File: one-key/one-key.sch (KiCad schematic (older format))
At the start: 8 parts, among them J2 Conn_01x04, SW1 SW_Push, U1 C8051F38x_32

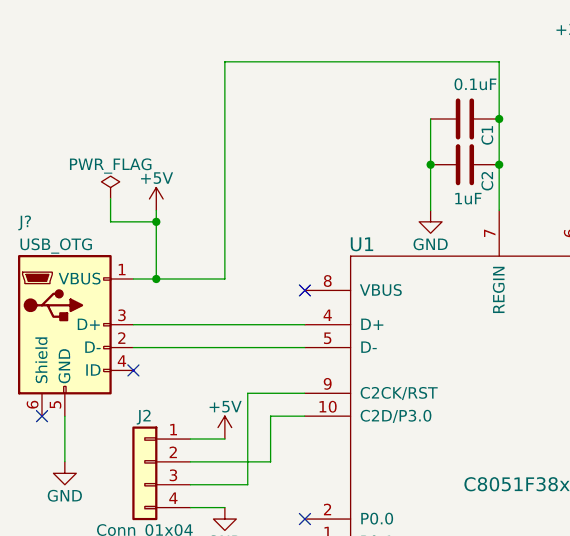
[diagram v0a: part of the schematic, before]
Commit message: vbus sense pin needs to be connected
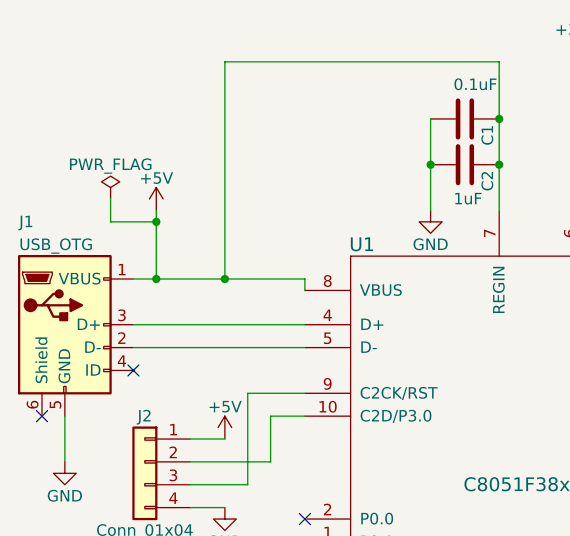
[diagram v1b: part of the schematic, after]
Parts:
- gave numbers to parts that had none: 1
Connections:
- net +5V: now also U1.8 (VBUS)
- no-connect marks 26 -> 25
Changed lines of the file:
@@
 $EndComp
 $Comp
-L GND #PWR01
+L GND #PWR9
 U 1 1 59BC69D8
 P 5000 1750
-F 0 "#PWR01" H 5000 1500 50  0001 C CNN
+F 0 "#PWR9" H 5000 1500 50  0001 C CNN
 F 1 "GND" H 5000 1600 50  0000 C CNN
 F 2 "" H 5000 1750 50  0001 C CNN
@@
 $EndComp
 $Comp
-L GND #PWR02
+L GND #PWR6
 U 1 1 59BC6AED
 P 4050 1750
-F 0 "#PWR02" H 4050 1500 50  0001 C CNN
+F 0 "#PWR6" H 4050 1500 50  0001 C CNN
 F 1 "GND" H 4050 1600 50  0000 C CNN
 F 2 "" H 4050 1750 50  0001 C CNN
@@
 $EndComp
 $Comp
-L +3.3V #PWR03
+L +3.3V #PWR8
 U 1 1 59BC6B24
 P 4700 1100
-F 0 "#PWR03" H 4700 950 50  0001 C CNN
+F 0 "#PWR8" H 4700 950 50  0001 C CNN
 F 1 "+3.3V" H 4700 1240 50  0000 C CNN
 F 2 "" H 4700 1100 50  0001 C CNN
@@
 NoConn ~ 2350 2650
 $Comp
-L GND #PWR04
+L GND #PWR1
 U 1 1 59BC6CDD
 P 2450 2850
-F 0 "#PWR04" H 2450 2600 50  0001 C CNN
+F 0 "#PWR1" H 2450 2600 50  0001 C CNN
 F 1 "GND" H 2450 2700 50  0000 C CNN
 F 2 "" H 2450 2850 50  0001 C CNN
@@
 	1    0    0    -1
 $EndComp
-NoConn ~ 3500 2100
-$Comp
-L GND #PWR05
+$Comp
+L GND #PWR7
 U 1 1 59BC6D91
 P 4500 4350
-F 0 "#PWR05" H 4500 4100 50  0001 C CNN
+F 0 "#PWR7" H 4500 4100 50  0001 C CNN
 F 1 "GND" H 4500 4200 50  0000 C CNN
 F 2 "" H 4500 4350 50  0001 C CNN
@@
 $EndComp
 $Comp
-L GND #PWR06
+L GND #PWR5
 U 1 1 59BC8562
 P 3150 3050
-F 0 "#PWR06" H 3150 2800 50  0001 C CNN
+F 0 "#PWR5" H 3150 2800 50  0001 C CNN
 F 1 "GND" H 3150 2900 50  0000 C CNN
 F 2 "" H 3150 3050 50  0001 C CNN
@@
 $EndComp
 $Comp
-L GND #PWR07
+L GND #PWR2
 U 1 1 59BC8C94
 P 2500 3800
-F 0 "#PWR07" H 2500 3550 50  0001 C CNN
+F 0 "#PWR2" H 2500 3550 50  0001 C CNN
 F 1 "GND" H 2500 3650 50  0000 C CNN
 F 2 "" H 2500 3800 50  0001 C CNN
@@
 	2500 3650 2500 3800
 $Comp
-L +5V #PWR08
+L +5V #PWR3
 U 1 1 59BC8F84
 P 2850 1750
-F 0 "#PWR08" H 2850 1600 50  0001 C CNN
+F 0 "#PWR3" H 2850 1600 50  0001 C CNN
 F 1 "+5V" H 2850 1890 50  0000 C CNN
 F 2 "" H 2850 1750 50  0001 C CNN
@@
 	3150 1100 3150 2050
 Wire Wire Line
-	3150 2050 2750 2050
+	2750 2050 3500 2050
 Wire Wire Line
 	2850 1750 2850 2050
 Connection ~ 2850 2050
 $Comp
-L PWR_FLAG #FLG09
+L PWR_FLAG #FLG1
 U 1 1 59BC904D
 P 2650 1700
-F 0 "#FLG09" H 2650 1775 50  0001 C CNN
+F 0 "#FLG1" H 2650 1775 50  0001 C CNN
 F 1 "PWR_FLAG" H 2650 1850 50  0000 C CNN
 F 2 "" H 2650 1700 50  0001 C CNN
@@
 Connection ~ 2850 1800
 $Comp
-L +5V #PWR010
+L +5V #PWR4
 U 1 1 59BC90F8
 P 3150 2750
-F 0 "#PWR010" H 3150 2600 50  0001 C CNN
+F 0 "#PWR4" H 3150 2600 50  0001 C CNN
 F 1 "+5V" H 3150 2890 50  0000 C CNN
 F 2 "" H 3150 2750 50  0001 C CNN
@@
 	3300 3200 3500 3200
 $Comp
-L USB_OTG J?
+L USB_OTG J1
 U 1 1 59BC971A
 P 2450 2250
-F 0 "J?" H 2250 2700 50  0000 L CNN
+F 0 "J1" H 2250 2700 50  0000 L CNN
 F 1 "USB_OTG" H 2250 2600 50  0000 L CNN
 F 2 "" H 2600 2200 50  0001 C CNN
@@
 	1    0    0    -1
 $EndComp
+Wire Wire Line
+	3500 2050 3500 2100
+Connection ~ 3150 2050
 $EndSCHEMATC

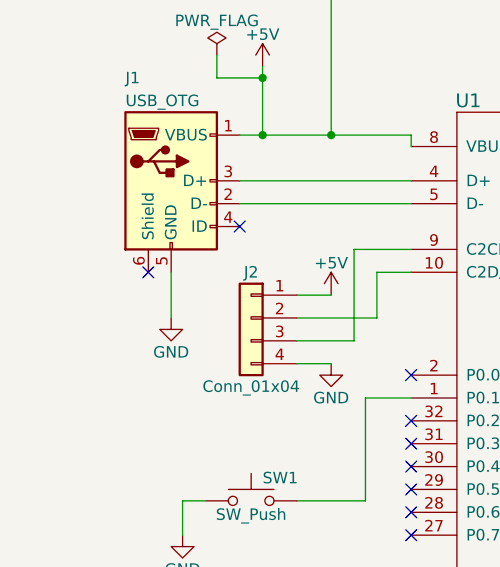
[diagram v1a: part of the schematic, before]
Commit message: add images and license text
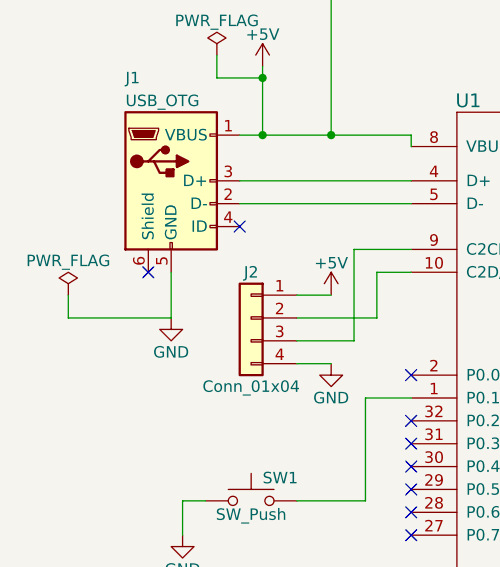
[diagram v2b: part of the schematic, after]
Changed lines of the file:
@@
 $EndComp
 $Comp
-L GND #PWR9
+L GND #PWR01
 U 1 1 59BC69D8
 P 5000 1750
-F 0 "#PWR9" H 5000 1500 50  0001 C CNN
+F 0 "#PWR01" H 5000 1500 50  0001 C CNN
 F 1 "GND" H 5000 1600 50  0000 C CNN
 F 2 "" H 5000 1750 50  0001 C CNN
@@
 $EndComp
 $Comp
-L GND #PWR6
+L GND #PWR02
 U 1 1 59BC6AED
 P 4050 1750
-F 0 "#PWR6" H 4050 1500 50  0001 C CNN
+F 0 "#PWR02" H 4050 1500 50  0001 C CNN
 F 1 "GND" H 4050 1600 50  0000 C CNN
 F 2 "" H 4050 1750 50  0001 C CNN
@@
 $EndComp
 $Comp
-L +3.3V #PWR8
+L +3.3V #PWR03
 U 1 1 59BC6B24
 P 4700 1100
-F 0 "#PWR8" H 4700 950 50  0001 C CNN
+F 0 "#PWR03" H 4700 950 50  0001 C CNN
 F 1 "+3.3V" H 4700 1240 50  0000 C CNN
 F 2 "" H 4700 1100 50  0001 C CNN
@@
 NoConn ~ 2350 2650
 $Comp
-L GND #PWR1
+L GND #PWR04
 U 1 1 59BC6CDD
 P 2450 2850
-F 0 "#PWR1" H 2450 2600 50  0001 C CNN
+F 0 "#PWR04" H 2450 2600 50  0001 C CNN
 F 1 "GND" H 2450 2700 50  0000 C CNN
 F 2 "" H 2450 2850 50  0001 C CNN
@@
 $EndComp
 $Comp
-L GND #PWR7
+L GND #PWR05
 U 1 1 59BC6D91
 P 4500 4350
-F 0 "#PWR7" H 4500 4100 50  0001 C CNN
+F 0 "#PWR05" H 4500 4100 50  0001 C CNN
 F 1 "GND" H 4500 4200 50  0000 C CNN
 F 2 "" H 4500 4350 50  0001 C CNN
@@
 $EndComp
 $Comp
-L GND #PWR5
+L GND #PWR06
 U 1 1 59BC8562
 P 3150 3050
-F 0 "#PWR5" H 3150 2800 50  0001 C CNN
+F 0 "#PWR06" H 3150 2800 50  0001 C CNN
 F 1 "GND" H 3150 2900 50  0000 C CNN
 F 2 "" H 3150 3050 50  0001 C CNN
@@
 $EndComp
 $Comp
-L GND #PWR2
+L GND #PWR07
 U 1 1 59BC8C94
 P 2500 3800
-F 0 "#PWR2" H 2500 3550 50  0001 C CNN
+F 0 "#PWR07" H 2500 3550 50  0001 C CNN
 F 1 "GND" H 2500 3650 50  0000 C CNN
 F 2 "" H 2500 3800 50  0001 C CNN
@@
 	2500 3650 2500 3800
 $Comp
-L +5V #PWR3
+L +5V #PWR08
 U 1 1 59BC8F84
 P 2850 1750
-F 0 "#PWR3" H 2850 1600 50  0001 C CNN
+F 0 "#PWR08" H 2850 1600 50  0001 C CNN
 F 1 "+5V" H 2850 1890 50  0000 C CNN
 F 2 "" H 2850 1750 50  0001 C CNN
@@
 Connection ~ 2850 2050
 $Comp
-L PWR_FLAG #FLG1
+L PWR_FLAG #FLG09
 U 1 1 59BC904D
 P 2650 1700
-F 0 "#FLG1" H 2650 1775 50  0001 C CNN
+F 0 "#FLG09" H 2650 1775 50  0001 C CNN
 F 1 "PWR_FLAG" H 2650 1850 50  0000 C CNN
 F 2 "" H 2650 1700 50  0001 C CNN
@@
 Connection ~ 2850 1800
 $Comp
-L +5V #PWR4
+L +5V #PWR010
 U 1 1 59BC90F8
 P 3150 2750
-F 0 "#PWR4" H 3150 2600 50  0001 C CNN
+F 0 "#PWR010" H 3150 2600 50  0001 C CNN
 F 1 "+5V" H 3150 2890 50  0000 C CNN
 F 2 "" H 3150 2750 50  0001 C CNN
@@
 	3500 2050 3500 2100
 Connection ~ 3150 2050
+$Comp
+L PWR_FLAG #FLG011
+U 1 1 59BDFC11
+P 2000 2750
+F 0 "#FLG011" H 2000 2825 50  0001 C CNN
+F 1 "PWR_FLAG" H 2000 2900 50  0000 C CNN
+F 2 "" H 2000 2750 50  0001 C CNN
+F 3 "" H 2000 2750 50  0001 C CNN
+	1    2000 2750
+	1    0    0    -1
+$EndComp
+Wire Wire Line
+	2000 2750 2000 2850
+Wire Wire Line
+	2000 2850 2450 2850
 $EndSCHEMATC
